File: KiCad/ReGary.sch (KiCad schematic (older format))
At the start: 10 parts, among them U4 SN74CBT16210, U5 SN74CBT16210, U6 SN74CBT16210, U7 SN74CBT16210, U8 PLCC_84_plug, U9 PLCC_84_plug

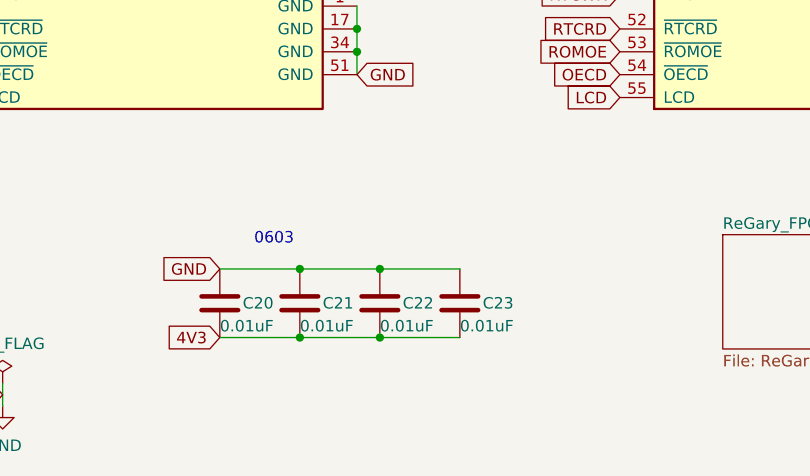
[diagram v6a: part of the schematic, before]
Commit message: Fixed JTAGSEL_N header size and silkscreen placement
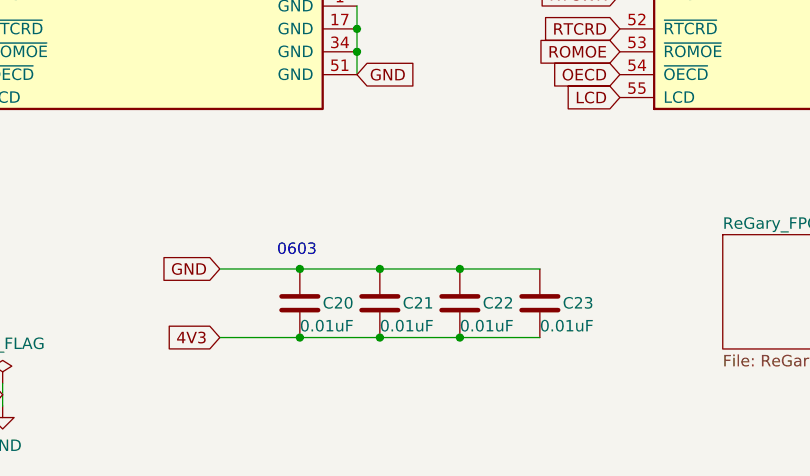
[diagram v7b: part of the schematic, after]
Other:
- moved on the sheet: C20, C21, C22, C23
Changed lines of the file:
@@
 	2500 6850 2850 6850
 Wire Wire Line
-	2150 7150 2500 7150
-Connection ~ 2500 7150
-Wire Wire Line
 	2500 7150 2850 7150
+Connection ~ 2850 7150
+Wire Wire Line
+	2850 7150 3200 7150
 Connection ~ 2850 6850
-Connection ~ 2850 7150
+Connection ~ 3200 7150
 Wire Wire Line
 	10200 1050 10200 950
@@
 	2850 6850 3200 6850
 Wire Wire Line
-	2850 7150 3200 7150
-Text Notes 2300 6750 0    50   ~ 0
+	3200 7150 3550 7150
+Text Notes 2400 6800 0    50   ~ 0
 0603
 $Comp
 L Device:C C23
 U 1 1 605F0F7B
+P 3550 7000
+F 0 "C23" H 3650 7000 50  0000 L CNN
+F 1 "0.01uF" H 3550 6900 50  0000 L CNN
+F 2 "Capacitor_SMD:C_0603_1608Metric_Pad1.05x0.95mm_HandSolder" H 3588 6850 50  0001 C CNN
+F 3 "~" H 3550 7000 50  0001 C CNN
+	1    3550 7000
+	1    0    0    -1
+$EndComp
+$Comp
+L Device:C C22
+U 1 1 605D5D6F
 P 3200 7000
-F 0 "C23" H 3300 7000 50  0000 L CNN
+F 0 "C22" H 3300 7000 50  0000 L CNN
 F 1 "0.01uF" H 3200 6900 50  0000 L CNN
 F 2 "Capacitor_SMD:C_0603_1608Metric_Pad1.05x0.95mm_HandSolder" H 3238 6850 50  0001 C CNN
@@
 $EndComp
 $Comp
-L Device:C C22
-U 1 1 605D5D6F
+L Device:C C21
+U 1 1 605D5659
 P 2850 7000
-F 0 "C22" H 2950 7000 50  0000 L CNN
+F 0 "C21" H 2950 7000 50  0000 L CNN
 F 1 "0.01uF" H 2850 6900 50  0000 L CNN
 F 2 "Capacitor_SMD:C_0603_1608Metric_Pad1.05x0.95mm_HandSolder" H 2888 6850 50  0001 C CNN
@@
 $EndComp
 $Comp
-L Device:C C21
-U 1 1 605D5659
+L Device:C C20
+U 1 1 605D3E60
 P 2500 7000
-F 0 "C21" H 2600 7000 50  0000 L CNN
+F 0 "C20" H 2600 7000 50  0000 L CNN
 F 1 "0.01uF" H 2500 6900 50  0000 L CNN
 F 2 "Capacitor_SMD:C_0603_1608Metric_Pad1.05x0.95mm_HandSolder" H 2538 6850 50  0001 C CNN
 F 3 "~" H 2500 7000 50  0001 C CNN
 	1    2500 7000
-	1    0    0    -1
-$EndComp
-$Comp
-L Device:C C20
-U 1 1 605D3E60
-P 2150 7000
-F 0 "C20" H 2250 7000 50  0000 L CNN
-F 1 "0.01uF" H 2150 6900 50  0000 L CNN
-F 2 "Capacitor_SMD:C_0603_1608Metric_Pad1.05x0.95mm_HandSolder" H 2188 6850 50  0001 C CNN
-F 3 "~" H 2150 7000 50  0001 C CNN
-	1    2150 7000
 	1    0    0    -1
 $EndComp
@@
 Text GLabel 10200 2950 2    50   Output ~ 0
 A23_FPGA
+Wire Wire Line
+	3550 6850 3200 6850
+Connection ~ 3200 6850
+Wire Wire Line
+	2500 7150 2150 7150
+Connection ~ 2500 7150
 $EndSCHEMATC

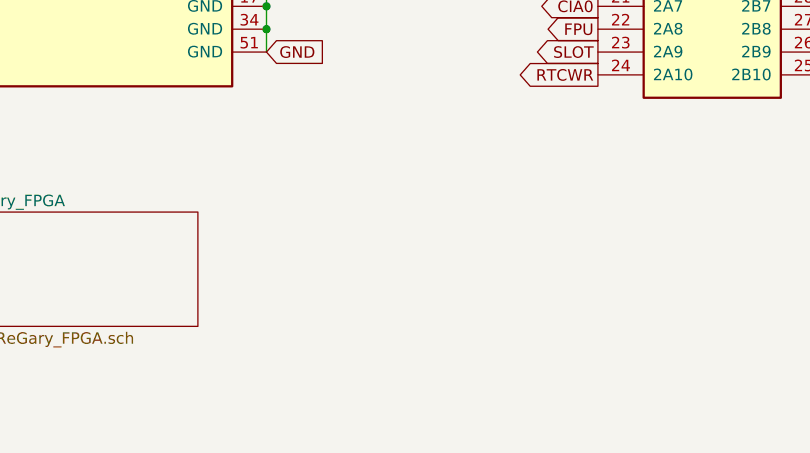
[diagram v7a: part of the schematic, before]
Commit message: Add a pin-header (with RW, A21, A20, A19 signals) for a built in Romy
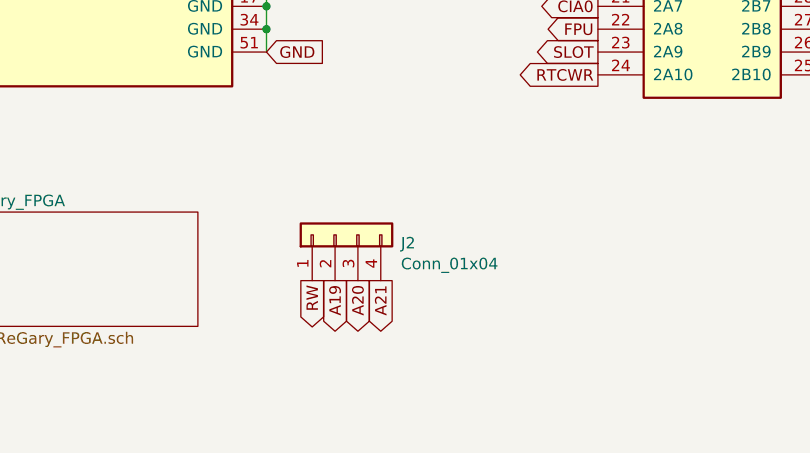
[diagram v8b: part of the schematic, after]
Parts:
- added J2: Conn_01x04, Connector_PinHeader_1.27mm:PinHeader_1x04_P1.27mm_Vertical, symbol Connector_Generic:Conn_01x04
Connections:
- net A19: now also J2.2 (Pin_2)
- net A20: now also J2.3 (Pin_3)
- net A21: now also J2.4 (Pin_4)
- net RW: now also J2.1 (Pin_1)
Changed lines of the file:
@@
 	2500 7150 2150 7150
 Connection ~ 2500 7150
+$Comp
+L Connector_Generic:Conn_01x04 J2
+U 1 1 6883696B
+P 6000 6800
+F 0 "J2" V 5964 6512 50  0000 R CNN
+F 1 "Conn_01x04" V 5873 6512 50  0000 R CNN
+F 2 "Connector_PinHeader_1.27mm:PinHeader_1x04_P1.27mm_Vertical" H 6000 6800 50  0001 C CNN
+F 3 "~" H 6000 6800 50  0001 C CNN
+	1    6000 6800
+	0    -1   -1   0
+$EndComp
+Text GLabel 6000 7000 3    50   Output ~ 0
+A19
+Text GLabel 6100 7000 3    50   Output ~ 0
+A20
+Text GLabel 5900 7000 3    50   Output ~ 0
+RW
+Text GLabel 6200 7000 3    50   Output ~ 0
+A21
 $EndSCHEMATC
